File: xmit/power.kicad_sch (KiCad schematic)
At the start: 6 parts, among them U1 74LVC1G66, U2 74LVC1G66, U3 74LVC1G66, U4 74LVC1G66, U5 74LVC1G66, U6 74LVC1G66

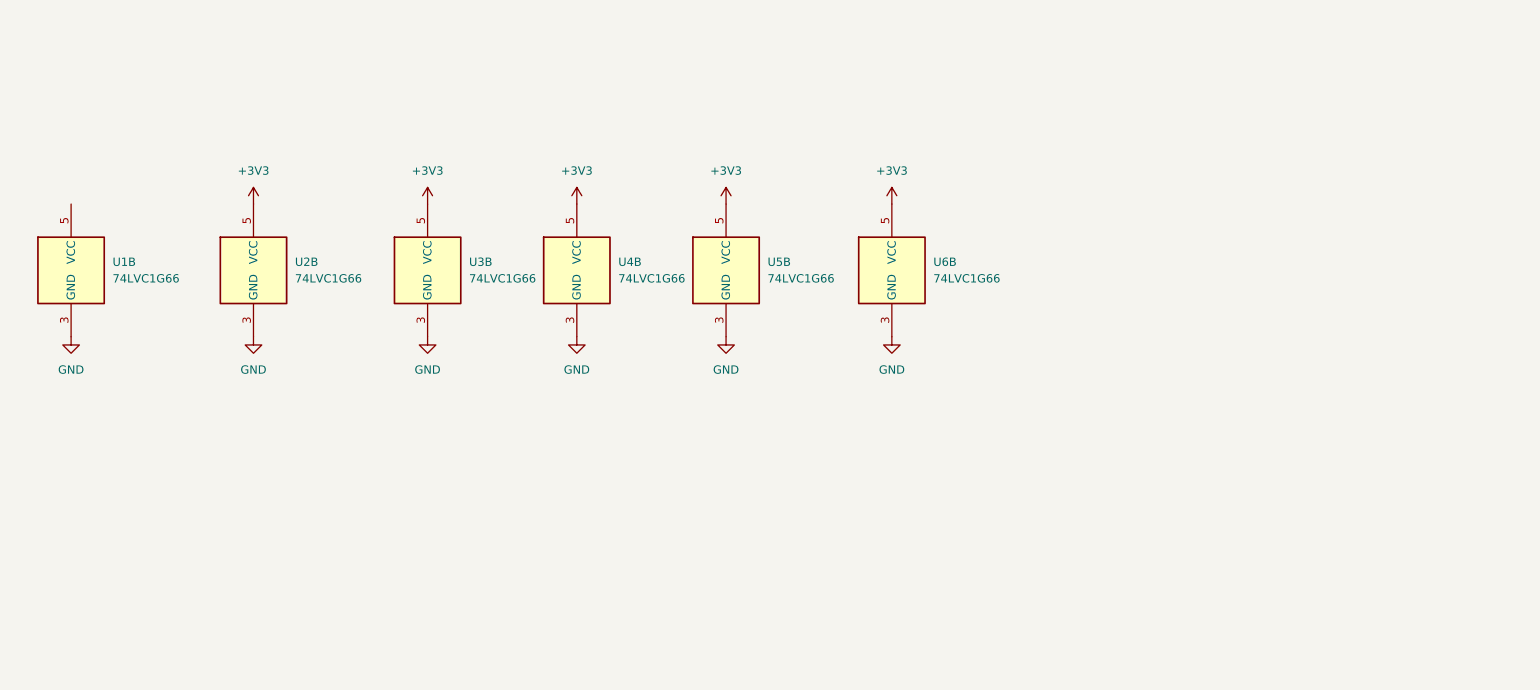
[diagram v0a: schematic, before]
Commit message: WIP commit, but the circuit is nearly done and PCB is beginning for form.
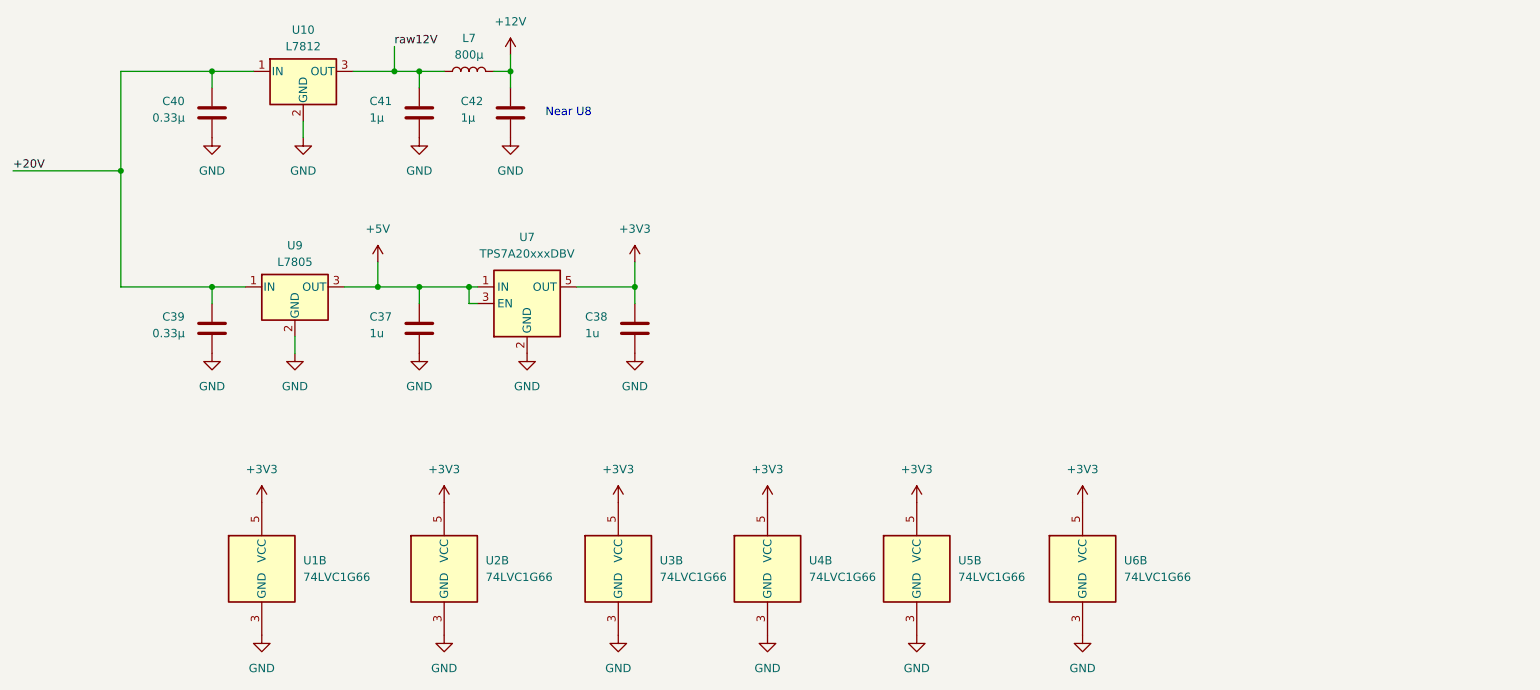
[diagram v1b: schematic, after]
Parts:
- added C37, C38: 1u, Capacitor_SMD:C_0805_2012Metric, symbol Device:C
- added C39, C40: 0.33µ, Capacitor_SMD:C_0805_2012Metric, symbol Device:C
- added C41, C42: 1µ, Capacitor_SMD:C_0805_2012Metric, symbol Device:C
- added L7: 800µ, Inductor_SMD:L_0805_2012Metric_Pad1.05x1.20mm_HandSolder, symbol Device:L
- added U10: L7812, Package_TO_SOT_THT:TO-220-3_Horizontal_TabDown, symbol Regulator_Linear:L7812
- added U7: TPS7A20xxxDBV, Package_TO_SOT_SMD:SOT-23-5, symbol Regulator_Linear:TPS7A20xxxDBV
- added U9: L7805, Package_TO_SOT_THT:TO-220-3_Horizontal_TabDown, symbol Regulator_Linear:L7805
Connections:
- net +3V3: now also U1.5 (VCC), C38.2, U7.5 (OUT)
- net GND: now also C37.1, C38.1, C39.1, C40.1, C41.1, C42.1, U10.2 (GND), U7.2 (GND), U9.2 (GND)
- new net +12V: C42.2, L7.2
- new net +20V: C39.2, C40.2, U10.1 (IN), U9.1 (IN)
- new net +5V: C37.2, U7.1 (IN), U7.3 (EN), U9.3 (OUT)
- new net raw12V: C41.2, L7.1, U10.3 (OUT)
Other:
- note added: "Near U8"
- moved on the sheet: U1B, U2B, U3B, U4B, U5B, U6B

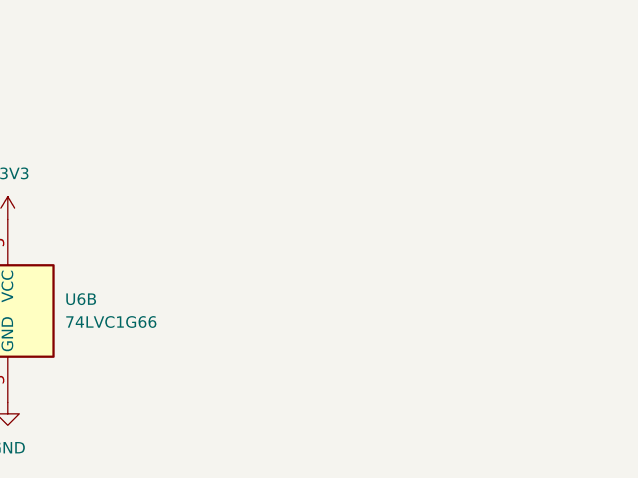
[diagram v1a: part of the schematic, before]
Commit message: Updated filters and improved amp
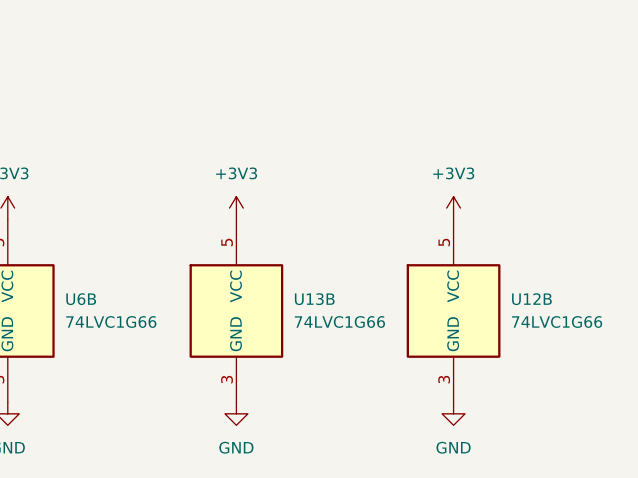
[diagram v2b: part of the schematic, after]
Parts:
- added U12, U13: 74LVC1G66, Package_TO_SOT_SMD:SOT-23-5_HandSoldering, symbol 74xGxx:74LVC1G66
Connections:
- net +3V3: now also U12.5 (VCC), U13.5 (VCC)
- net GND: now also U12.3 (GND), U13.3 (GND)

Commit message: Another WIP on transmitter layout. Should be pretty close.
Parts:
- U9: value L7805 -> TLV760; footprint Package_TO_SOT_THT:TO-220-3_Horizontal_TabDown -> Package_TO_SOT_SMD:TSOT-23
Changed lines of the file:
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@@
 			)
 		)
-		(property "Value" "L7805"
+		(property "Value" "TLV760"
 			(at 88.9 57.15 0)
 			(show_name no)
@@
 			)
 		)
-		(property "Footprint" "Package_TO_SOT_THT:TO-220-3_Horizontal_TabDown"
+		(property "Footprint" "Package_TO_SOT_SMD:TSOT-23"
 			(at 89.535 64.77 0)
 			(hide yes)
@@
 			)
 		)
-		(property "Datasheet" "http://www.st.com/content/ccc/resource/technical/document/datasheet/41/4f/b3/b0/12/d4/47/88/CD00000444.pdf/files/CD00000444.pdf/jcr:content/translations/en.CD00000444.pdf"
+		(property "Datasheet" "https://www.ti.com/lit/ds/symlink/tlv760.pdf"
 			(at 88.9 62.23 0)
 			(hide yes)
@@
 			)
 		)
-		(property "Description" "Positive 1.5A 35V Linear Regulator, Fixed Output 5V, TO-220/TO-263/TO-252"
+		(property "Description" ""
 			(at 88.9 60.96 0)
 			(hide yes)
